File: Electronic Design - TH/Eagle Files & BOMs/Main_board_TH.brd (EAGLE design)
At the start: 90 x 137 mm, 41 parts, among them M1 ARDUINO-NANO-3.0, Q1 IRF9520, Q2 IRF9520

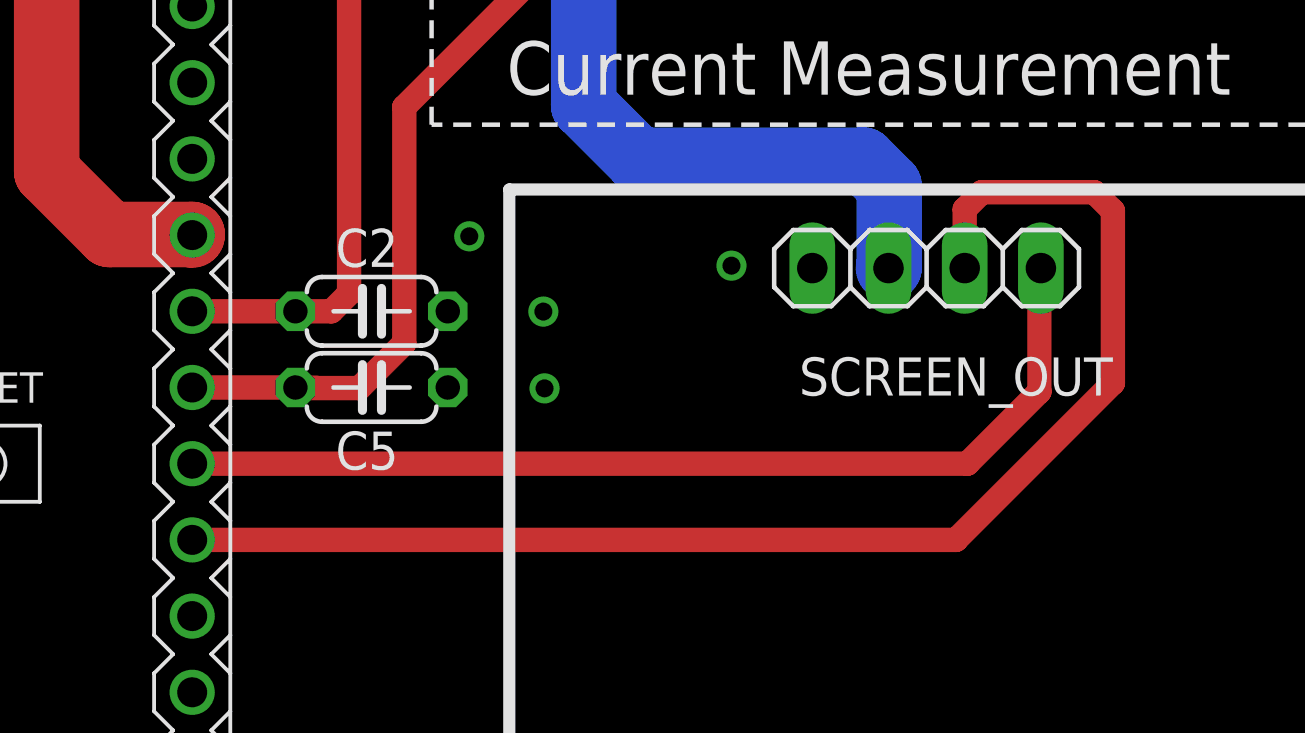
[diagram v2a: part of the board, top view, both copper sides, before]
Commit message: updating firmware and correcting screen pins
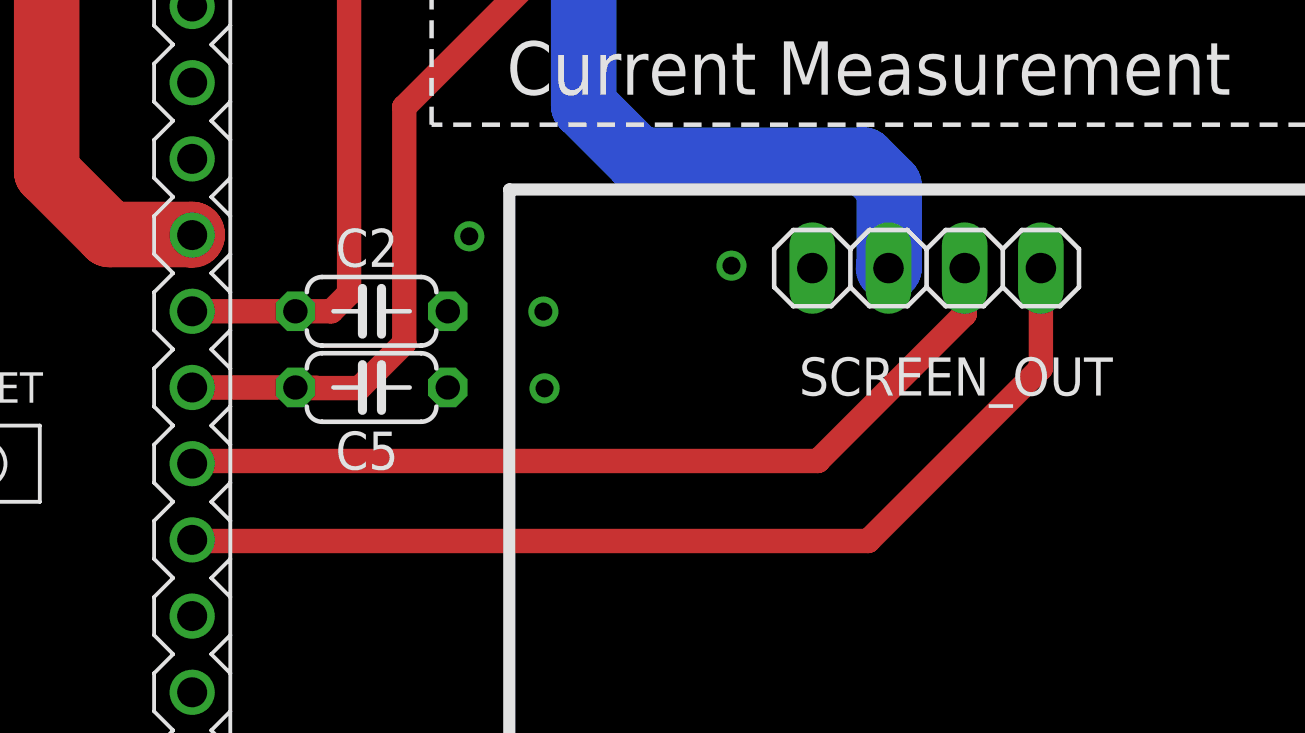
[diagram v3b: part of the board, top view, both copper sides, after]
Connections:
- removed net A4: M1.J2.8, SCREEN_OUT.2
- removed net A5: M1.J2.7, SCREEN_OUT.1
- new net N$11: M1.J2.7, SCREEN_OUT.2
- new net N$12: M1.J2.8, SCREEN_OUT.1
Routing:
- net A4: track 46.0 -> 0.00 mm
- net N$12: track 0.00 -> 34.0 mm
- net A5: track 33.4 -> 0.00 mm
- net N$11: track 0.00 -> 29.4 mm
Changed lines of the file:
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@@
 <vertex x="-2.47" y="137.93"/>
 </polygon>
+<wire x1="77.06569375" y1="124.1102" x2="80.0402" y2="124.06430625" width="0" layer="19" extent="1-1"/>
+<wire x1="74.51" y1="124.07" x2="77.06569375" y2="124.1102" width="0" layer="19" extent="1-1"/>
+<wire x1="80.04186875" y1="121.065390625" x2="80.0402" y2="124.06430625" width="0" layer="19" extent="1-1"/>
+<wire x1="77.06" y1="121.07" x2="80.04186875" y2="121.065390625" width="0" layer="19" extent="1-1"/>
+<wire x1="75.98569375" y1="108.3602" x2="77.06" y2="121.07" width="0" layer="19" extent="1-1"/>
+<wire x1="73.15" y1="108.278" x2="75.98569375" y2="108.3602" width="0" layer="19" extent="1-1"/>
+<wire x1="70.52569375" y1="108.2702" x2="73.15" y2="108.278" width="0" layer="19" extent="1-1"/>
+<wire x1="66.01569375" y1="108.2302" x2="70.52569375" y2="108.2702" width="0" layer="19" extent="1-1"/>
+<wire x1="54.94709375" y1="118.1762" x2="66.01569375" y2="108.2302" width="0" layer="19" extent="1-1"/>
+<wire x1="52.62" y1="122" x2="54.94709375" y2="118.1762" width="0" layer="19" extent="1-1"/>
+<wire x1="57.89569375" y1="122.2302" x2="54.94709375" y2="118.1762" width="0" layer="19" extent="1-1"/>
+<wire x1="52.67569375" y1="128.1902" x2="52.62" y2="122" width="0" layer="19" extent="1-1"/>
+<wire x1="50.08" y1="90.46" x2="66.01569375" y2="108.2302" width="0" layer="19" extent="1-1"/>
+<wire x1="50.08" y1="85.38" x2="50.08" y2="90.46" width="0" layer="19" extent="1-1"/>
+<wire x1="52.62" y1="75.5" x2="50.08" y2="85.38" width="0" layer="19" extent="1-1"/>
+<wire x1="55.61569375" y1="75.6302" x2="52.62" y2="75.5" width="0" layer="19" extent="1-1"/>
+<wire x1="58.62569375" y1="75.6302" x2="55.61569375" y2="75.6302" width="0" layer="19" extent="1-1"/>
+<wire x1="56.43" y1="72" x2="55.61569375" y2="75.6302" width="0" layer="19" extent="1-1"/>
+<wire x1="56.22569375" y1="66.7202" x2="56.43" y2="72" width="0" layer="19" extent="1-1"/>
+<wire x1="56.01" y1="63.11" x2="56.22569375" y2="66.7202" width="0" layer="19" extent="1-1"/>
+<wire x1="59.78569375" y1="64.9702" x2="56.22569375" y2="66.7202" width="0" layer="19" extent="1-1"/>
+<wire x1="51.42569375" y1="62.3502" x2="56.01" y2="63.11" width="0" layer="19" extent="1-1"/>
+<wire x1="53.21149375" y1="53.5762" x2="51.42569375" y2="62.3502" width="0" layer="19" extent="1-1"/>
+<wire x1="53.11569375" y1="50.9902" x2="53.21149375" y2="53.5762" width="0" layer="19" extent="1-1"/>
+<wire x1="50.08" y1="51" x2="53.11569375" y2="50.9902" width="0" layer="19" extent="1-1"/>
+<wire x1="49.84569375" y1="53.5302" x2="50.08" y2="51" width="0" layer="19" extent="1-1"/>
+<wire x1="41.19" y1="65.65" x2="51.42569375" y2="62.3502" width="0" layer="19" extent="1-1"/>
+<wire x1="38.63569375" y1="65.8502" x2="41.19" y2="65.65" width="0" layer="19" extent="1-1"/>
+<wire x1="36.11" y1="56.76" x2="38.63569375" y2="65.8502" width="0" layer="19" extent="1-1"/>
+<wire x1="41.19" y1="40.72" x2="50.08" y2="51" width="0" layer="19" extent="1-1"/>
+<wire x1="38.49569375" y1="40.8002" x2="41.19" y2="40.72" width="0" layer="19" extent="1-1"/>
+<wire x1="32.22569375" y1="39.2702" x2="38.49569375" y2="40.8002" width="0" layer="19" extent="1-1"/>
+<wire x1="32.26569375" y1="36.7102" x2="32.22569375" y2="39.2702" width="0" layer="19" extent="1-1"/>
+<wire x1="29.04" y1="39.28" x2="32.22569375" y2="39.2702" width="0" layer="19" extent="1-1"/>
+<wire x1="29.04" y1="36.74" x2="29.04" y2="39.28" width="0" layer="19" extent="1-1"/>
+<wire x1="29.75569375" y1="41.7802" x2="29.04" y2="39.28" width="0" layer="19" extent="1-1"/>
+<wire x1="20.52" y1="46.9" x2="29.75569375" y2="41.7802" width="0" layer="19" extent="1-1"/>
+<wire x1="10.49569375" y1="59.5302" x2="20.52" y2="46.9" width="0" layer="19" extent="1-1"/>
+<wire x1="8" y1="61.73" x2="10.49569375" y2="59.5302" width="0" layer="19" extent="1-1"/>
+<wire x1="13.13" y1="63" x2="10.49569375" y2="59.5302" width="0" layer="19" extent="1-1"/>
+<wire x1="14.37569375" y1="65.4302" x2="13.13" y2="63" width="0" layer="19" extent="1-1"/>
+<wire x1="9.32" y1="71.48" x2="14.37569375" y2="65.4302" width="0" layer="19" extent="1-1"/>
+<wire x1="9.14569375" y1="73.9602" x2="9.32" y2="71.48" width="0" layer="19" extent="1-1"/>
+<wire x1="17.41569375" y1="73.8702" x2="9.14569375" y2="73.9602" width="0" layer="19" extent="1-1"/>
+<wire x1="19.48" y1="76.56" x2="17.41569375" y2="73.8702" width="0" layer="19" extent="1-1"/>
+<wire x1="13.13" y1="91.57" x2="19.48" y2="76.56" width="0" layer="19" extent="1-1"/>
+<wire x1="9.25569375" y1="91.5202" x2="13.13" y2="91.57" width="0" layer="19" extent="1-1"/>
+<wire x1="9.41569375" y1="94.5502" x2="9.25569375" y2="91.5202" width="0" layer="19" extent="1-1"/>
+<wire x1="20.54569375" y1="118.8802" x2="9.41569375" y2="94.5502" width="0" layer="19" extent="1-1"/>
+<wire x1="24.49569375" y1="121.6002" x2="20.54569375" y2="118.8802" width="0" layer="19" extent="1-1"/>
+<wire x1="25.389" y1="118.81" x2="24.49569375" y2="121.6002" width="0" layer="19" extent="1-1"/>
 </signal>
 <signal name="VIN_PROTECTED">
@@
 <wire x1="66.964" y1="23.506" x2="69.17" y2="21.3" width="2.1844" layer="1"/>
 </signal>
-<signal name="A5">
-<contactref element="SCREEN_OUT" pad="1"/>
-<contactref element="M1" pad="J2.7"/>
-<wire x1="20.52" y1="34.2" x2="46.36" y2="34.2" width="0.8128" layer="1"/>
-<wire x1="46.36" y1="34.2" x2="48.76" y2="36.6" width="0.8128" layer="1"/>
-<wire x1="48.76" y1="36.6" x2="48.76" y2="40.67" width="0.8128" layer="1"/>
-<wire x1="48.76" y1="40.67" x2="48.81" y2="40.72" width="0.8128" layer="1"/>
-</signal>
-<signal name="A4">
-<contactref element="M1" pad="J2.8"/>
-<contactref element="SCREEN_OUT" pad="2"/>
-<wire x1="46.27" y1="40.72" x2="46.27" y2="42.68" width="0.8128" layer="1"/>
-<wire x1="46.27" y1="42.68" x2="46.84" y2="43.25" width="0.8128" layer="1"/>
-<wire x1="46.84" y1="43.25" x2="50.59" y2="43.25" width="0.8128" layer="1"/>
-<wire x1="50.59" y1="43.25" x2="51.21" y2="42.63" width="0.8128" layer="1"/>
-<wire x1="51.21" y1="42.63" x2="51.21" y2="36.89" width="0.8128" layer="1"/>
-<wire x1="51.21" y1="36.89" x2="45.98" y2="31.66" width="0.8128" layer="1"/>
-<wire x1="45.98" y1="31.66" x2="20.52" y2="31.66" width="0.8128" layer="1"/>
-</signal>
 <signal name="N$2">
 <contactref element="R9" pad="1"/>
@@
 <wire x1="64.35" y1="124.07" x2="64.35" y2="114.53" width="2.1844" layer="1"/>
 </signal>
+<signal name="N$11">
+<contactref element="M1" pad="J2.7"/>
+<contactref element="SCREEN_OUT" pad="2"/>
+<wire x1="46.27" y1="40.72" x2="46.27" y2="39.1834" width="0.8128" layer="1"/>
+<wire x1="46.27" y1="39.1834" x2="41.3766" y2="34.29" width="0.8128" layer="1"/>
+<wire x1="41.3766" y1="34.29" x2="20.61" y2="34.29" width="0.8128" layer="1"/>
+<wire x1="20.61" y1="34.29" x2="20.52" y2="34.2" width="0.8128" layer="1"/>
+</signal>
+<signal name="N$12">
+<contactref element="M1" pad="J2.8"/>
+<contactref element="SCREEN_OUT" pad="1"/>
+<wire x1="48.81" y1="40.72" x2="48.81" y2="37.38" width="0.8128" layer="1"/>
+<wire x1="48.81" y1="37.38" x2="43.053" y2="31.623" width="0.8128" layer="1"/>
+<wire x1="43.053" y1="31.623" x2="20.557" y2="31.623" width="0.8128" layer="1"/>
+<wire x1="20.557" y1="31.623" x2="20.52" y2="31.66" width="0.8128" layer="1"/>
+</signal>
 </signals>

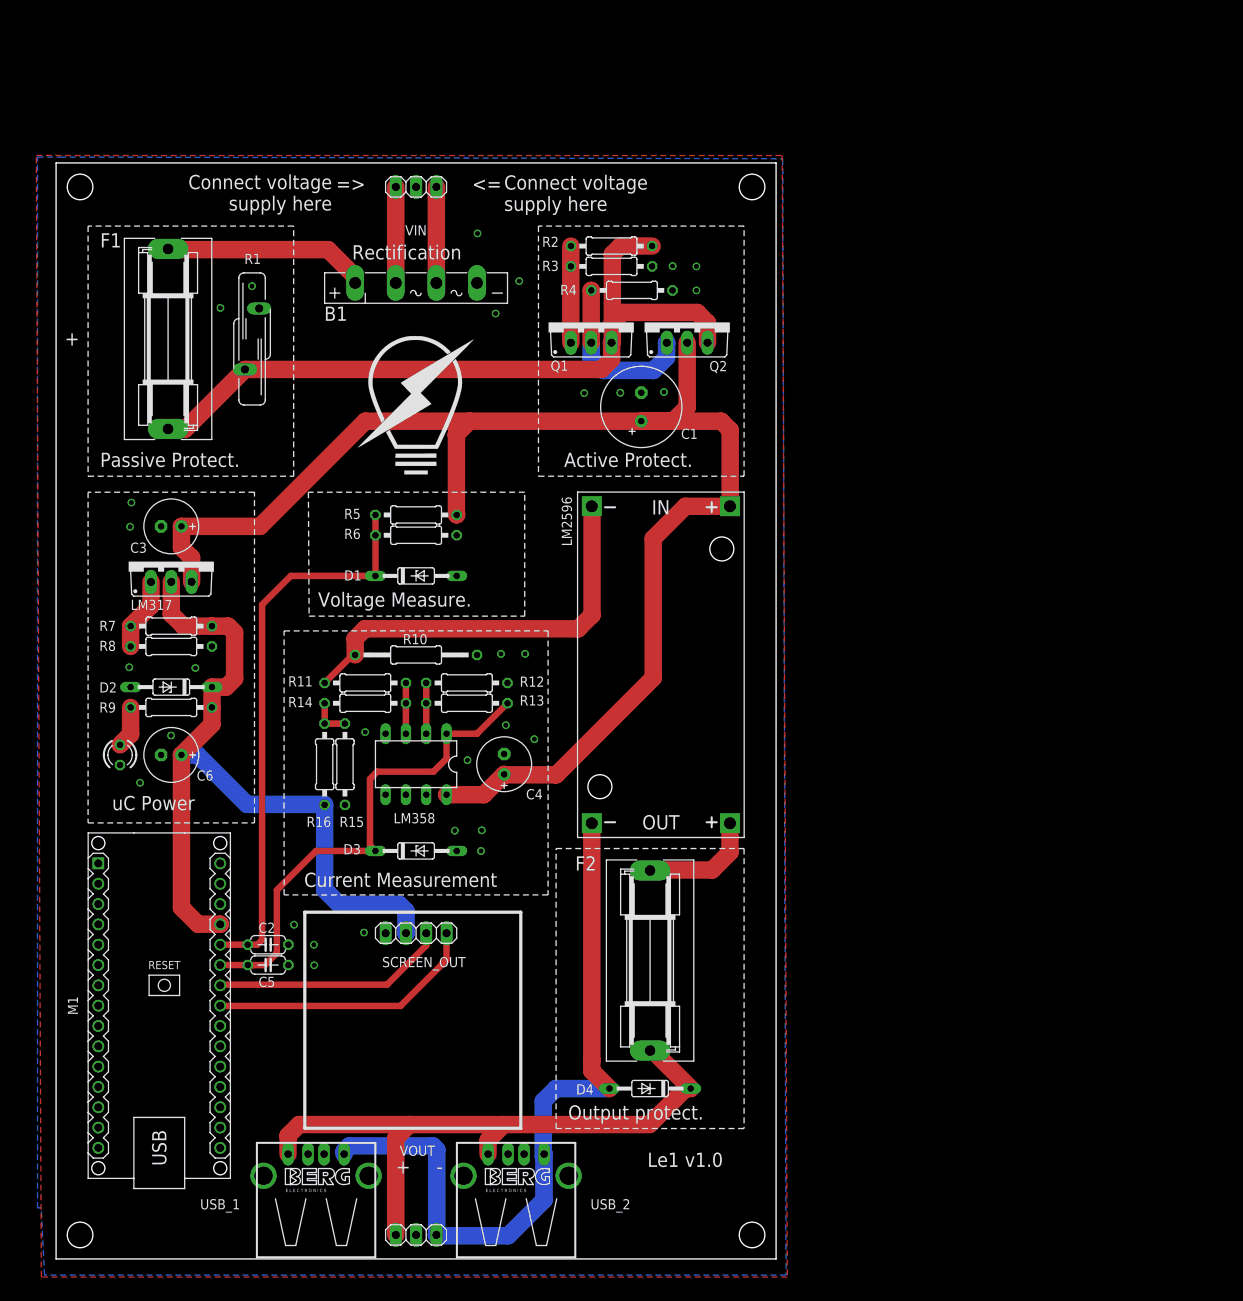
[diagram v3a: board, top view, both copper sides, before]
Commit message: adding in new LED for testing and widening board
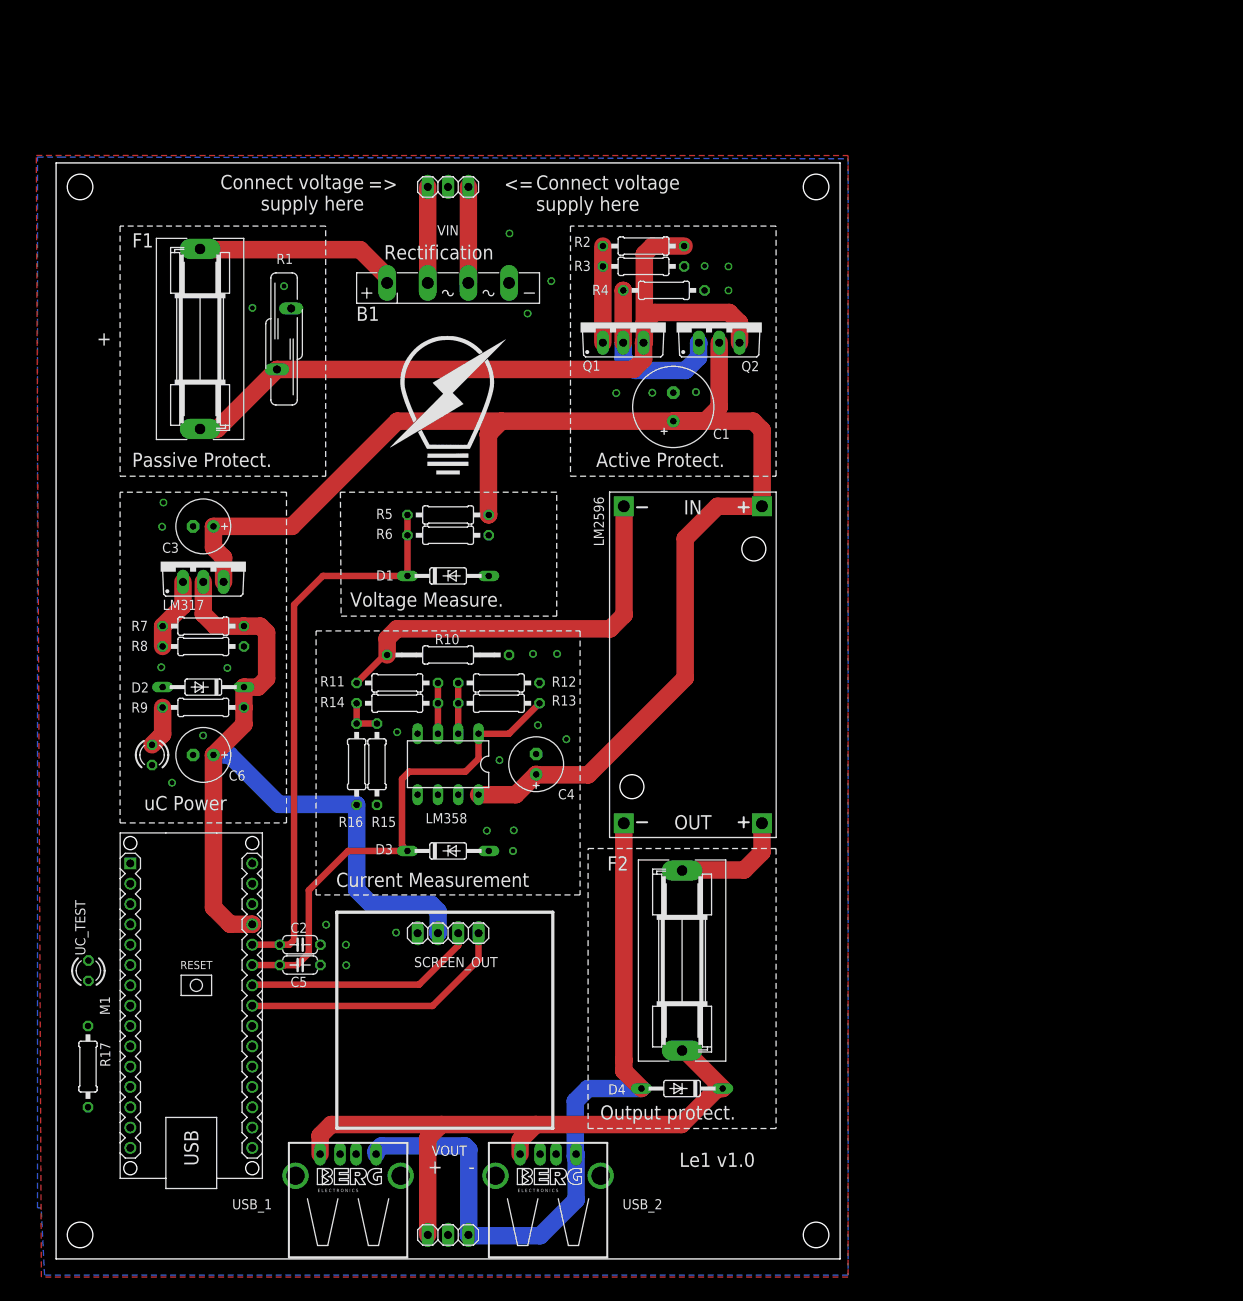
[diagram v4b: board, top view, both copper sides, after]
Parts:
- added R17: 2k, resistor:0207/10
- added UC_TEST: (no value), led:LED3MM
- moved B1 4.00 mm to (49.0, 122.0)
- moved C1 4.00 mm to (77.2, 106.5)
- moved C2 4.00 mm to (30.5, 39.3)
- moved C4 4.00 mm to (60.0, 61.8)
- moved C5 4.00 mm to (30.5, 36.7)
- moved D1 4.00 mm to (49.0, 85.4)
- moved D3 4.00 mm to (49.0, 51.0)
- moved D4 4.00 mm to (78.2, 21.3)
- moved F1 4.00 mm to (18.0, 115.0)
- moved F2 4.00 mm to (78.2, 37.3)
- moved LM2596 4.00 mm to (79.6, 74.3)
- moved LM358 4.00 mm to (49.0, 61.8)
- moved Q1 4.00 mm to (70.9, 117.1)
- moved Q2 4.00 mm to (82.9, 117.1)
- moved R1 4.00 mm to (28.5, 115.0)
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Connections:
- new net N$13: M1.J1.13, R17.2
- new net N$14: R17.1, UC_TEST.A
- net GND: now also UC_TEST.K
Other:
- board size 90 x 137 mm -> 98 x 137 mm
